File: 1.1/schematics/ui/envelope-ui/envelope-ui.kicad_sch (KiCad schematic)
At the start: 21 parts, among them U1 SW_SPST_Push_LED

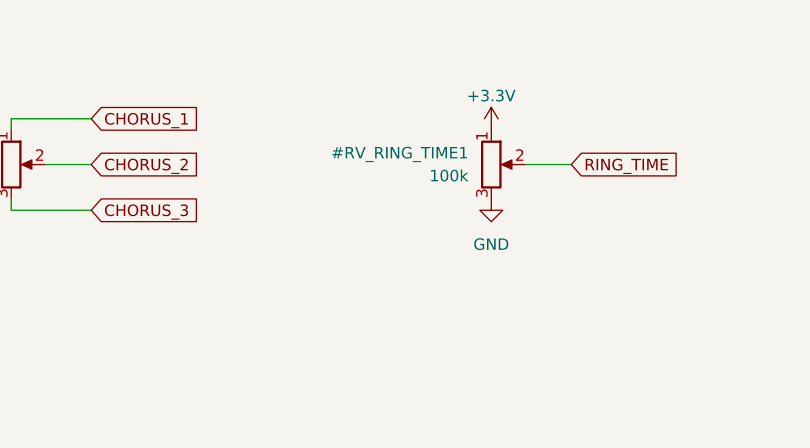
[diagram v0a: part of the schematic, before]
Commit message: Made envelope UI narrower
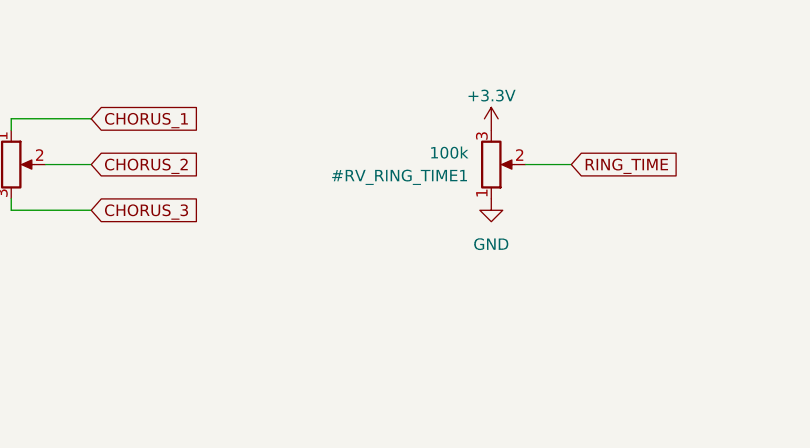
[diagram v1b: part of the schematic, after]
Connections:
- net +3.3V: now also #RV_RING_TIME1.3; no longer #RV_RING_TIME1.1
- net GND: now also #RV_RING_TIME1.1; no longer #RV_RING_TIME1.3
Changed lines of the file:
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@@
     )
   )
-  (symbol (lib_id "Device:R_Potentiometer") (at 167.64 50.8 0) (unit 1)
-    (in_bom yes) (on_board yes) (dnp no) (fields_autoplaced)
-    (property "Reference" "#RV_RING_TIME1" (at 165.1 49.53 0)
+  (symbol (lib_id "Device:R_Potentiometer") (at 167.64 50.8 0) (mirror x) (unit 1)
+    (in_bom yes) (on_board yes) (dnp no)
+    (property "Reference" "#RV_RING_TIME1" (at 165.1 52.07 0)
       (effects (font (size 1.27 1.27)) (justify right))
     )
-    (property "Value" "100k" (at 165.1 52.07 0)
+    (property "Value" "100k" (at 165.1 49.53 0)
       (effects (font (size 1.27 1.27)) (justify right))
     )

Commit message: Envelope UI refinements
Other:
- note added: "Note that the current is directly supplied from the Pico. The maximum suggested value is 16mA, so a 10mA current is sufficient. Resistor values for 10mA: BLUE - 100ohm GREEN - 220ohm RED - 220ohm"
- moved on the sheet: J_CHORUS1, J_PWR1, J_SND_SRC_UI_CONN1, J_UI2, J_UI3, R1, SW_HOLD_1A, SW_HOLD_1B, SW_RING_1A, SW_RING_1B, SW_SOFT_1A, SW_SOFT_1B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
